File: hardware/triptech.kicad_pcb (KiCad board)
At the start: 4 copper layers, 262.8 x 99.5 mm, 75 parts, among them J1 Conn_01x03_Pin, J2 GPIO Header, J4 NCJ6FA-H-0, J5 NCJ6FA-H-0, J6 Conn_01x04_Pin, J7 NCJ6FA-H-0, J8 NCJ6FA-H-0, Q1 SI2301CDS-T1-GE3, U1 TMA-1212D, U2 TPS54302, U3 Daisy_Seed, U4 H11L1SM, U5 THAT1246, U6 THAT1246, U7 THAT1646, U8 THAT1646

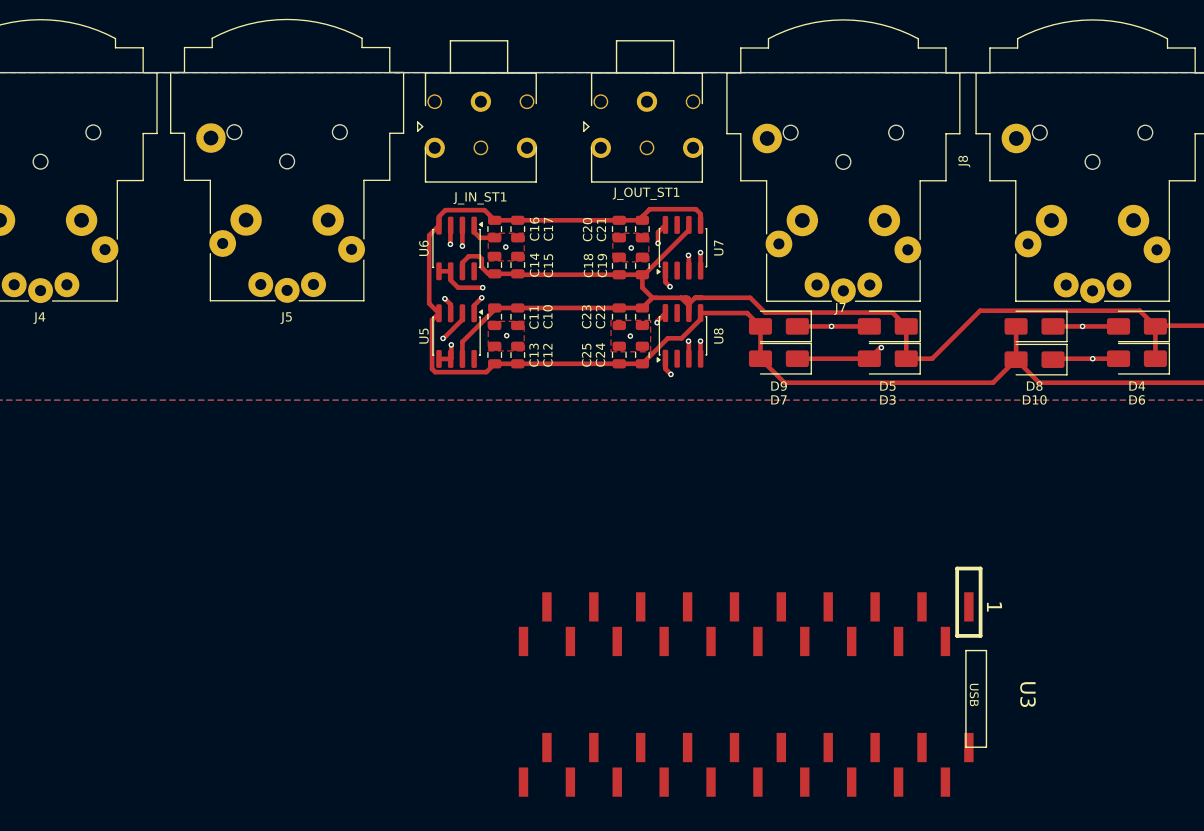
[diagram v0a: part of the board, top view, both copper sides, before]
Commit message: add protection circuit and repair pcb
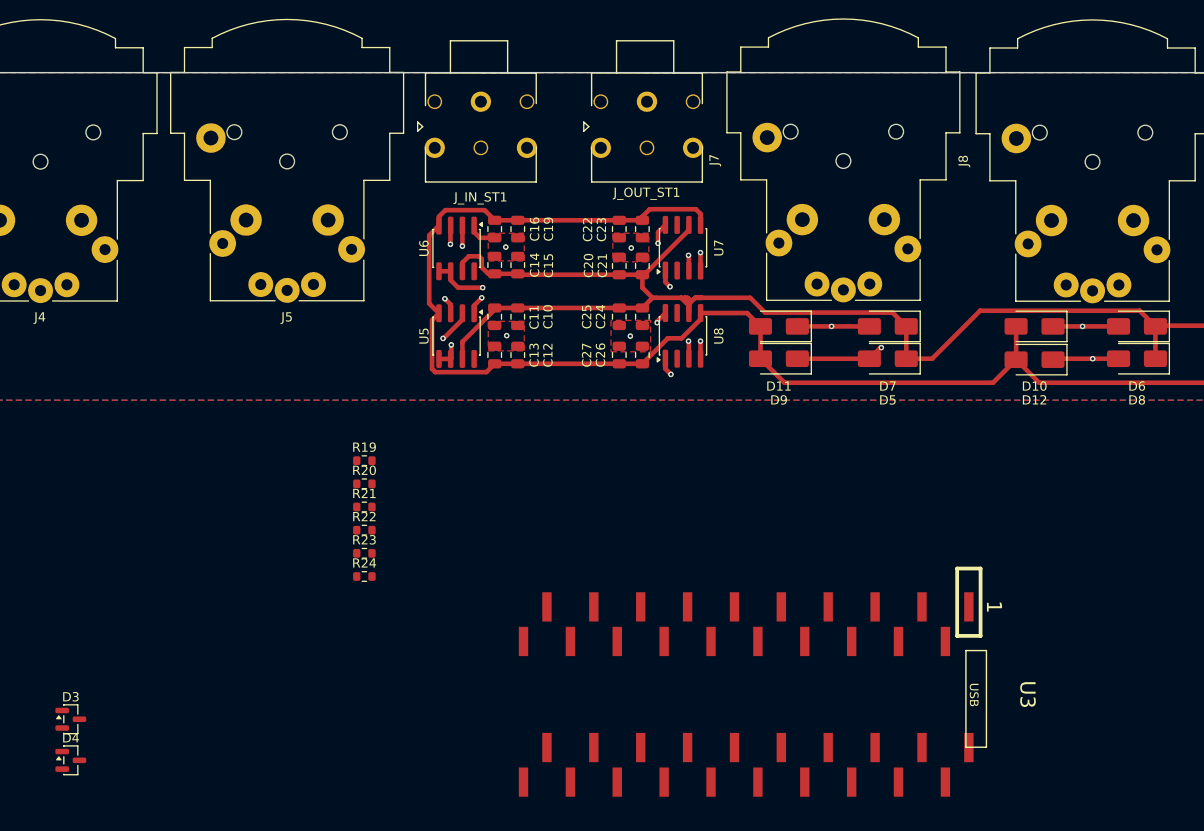
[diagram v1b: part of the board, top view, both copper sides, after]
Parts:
- added D3: BAT54S, Package_TO_SOT_SMD:SOT-23, F.Cu at (34.6, 90.1)
- added D4: BAT54S, Package_TO_SOT_SMD:SOT-23, F.Cu at (34.6, 94.5)
- added R19: 1.2k, Resistor_SMD:R_0603_1608Metric, F.Cu at (66.4, 62.0)
- added R20: 1.2k, Resistor_SMD:R_0603_1608Metric, F.Cu at (66.4, 64.6)
- added R21: 100k, Resistor_SMD:R_0603_1608Metric, F.Cu at (66.4, 67.1)
- added R22: 100k, Resistor_SMD:R_0603_1608Metric, F.Cu at (66.4, 69.6)
- added R23: 100k, Resistor_SMD:R_0603_1608Metric, F.Cu at (66.4, 72.1)
- added R24: 100k, Resistor_SMD:R_0603_1608Metric, F.Cu at (66.4, 74.6)
- moved J7 0.10 mm to (111.3, 38.5)
- renumbered C17 to C19, C18 to C20, C19 to C21, C20 to C22, C21 to C23, C22 to C24, C23 to C25, C24 to C26, C25 to C27, D8 to D10, D9 to D11, D10 to D12, D3 to D5, D4 to D6, D5 to D7, D6 to D8, D7 to D9
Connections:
- D11 pad 1: Net-(D5-A) (its old number) -> GNDA
- D12 pad 1: Net-(D10-K) (its old number) -> GNDA
- D7 pad 2: Net-(D5-A) (its old number) -> GNDA
- D8 pad 2: Net-(D10-K) (its old number) -> GNDA
- J7 pad 3: Net-(D5-A) (its old number) -> GNDA
- J7 pad R: Net-(D5-A) (its old number) -> GNDA
- J8 pad 3: Net-(D10-K) (its old number) -> GNDA
- J8 pad R: Net-(D10-K) (its old number) -> GNDA
- J_IN_ST1 pad 2: AUDIO_IN_L -> Net-(J_IN_ST1-T)
- J_IN_ST1 pad 5: AUDIO_IN_R -> Net-(J_IN_ST1-R)
- U5 pad 5: AUDIO_IN_L -> Net-(J_IN_ST1-T)
- U5 pad 6: AUDIO_IN_L -> Net-(J_IN_ST1-T)
- U6 pad 5: AUDIO_IN_R -> Net-(J_IN_ST1-R)
- U6 pad 6: AUDIO_IN_R -> Net-(J_IN_ST1-R)
- U7 pad 8: Net-(D5-A) (its old number) -> GNDA
- U8 pad 8: Net-(D10-K) (its old number) -> GNDA
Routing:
- net GNDA: track 8.79 -> 128.2 mm, vias 7 -> 11
- net Net-(D10-K) (its old number): track 75.3 -> 0.00 mm, vias 2 -> 0
- net Net-(D5-A) (its old number): track 44.0 -> 0.00 mm, vias 2 -> 0

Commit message: wip
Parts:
- added C17: 10u, Capacitor_SMD:C_0805_2012Metric, F.Cu at (35.8, 58.0)
- added C18: 10u, Capacitor_SMD:C_0805_2012Metric, F.Cu at (66.0, 54.5)
- added J_MIDI_IN1: SDS-50J, libs:SDS50J, F.Cu at (215.7, 38.7)
- added J_MIDI_OUT1: SDS-50J, libs:SDS50J, F.Cu at (192.9, 38.7)
- added J_MIDI_THRU1: SDS-50J, libs:SDS50J, F.Cu at (170.2, 38.7)
- added R25: 120R, Resistor_SMD:R_0603_1608Metric, F.Cu at (97.0, 39.8)
- added R26: 120R, Resistor_SMD:R_0603_1608Metric, F.Cu at (86.2, 39.7)
- added S1: LC2255EESP, libs:LC2255EESP, F.Cu at (90.2, 37.1)
- D2: value 1N4148WS -> 1N4148W; footprint Diode_SMD:D_SOD-323 -> Diode_SMD:D_SOD-123
- moved U3 128.6 mm to (258.1, 102.6)
- moved J6 72.8 mm to (90.3, 43.9)
- moved R8 68.0 mm to (255.4, 97.8), turned to -90 degrees
- moved C9 67.7 mm to (235.8, 45.8), turned to -90 degrees
- moved R7 66.3 mm to (252.8, 97.9), turned to -90 degrees
- moved R11 59.9 mm to (250.5, 97.7), turned to -90 degrees
- moved R10 59.4 mm to (247.9, 97.8), turned to -90 degrees
- moved C10 58.8 mm to (25.9, 60.5), turned to 90 degrees
- moved U4 58.4 mm to (229.9, 46.5)
- moved R9 57.5 mm to (245.3, 97.7), turned to -90 degrees
- moved C12 57.4 mm to (25.9, 56.5), turned to 90 degrees
- moved D2 55.8 mm to (219.2, 45.4)
- moved U5 55.3 mm to (22.0, 58.5)
- moved C11 54.3 mm to (28.1, 60.5), turned to 90 degrees
- moved C13 52.8 mm to (28.1, 56.5), turned to 90 degrees
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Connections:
- R13 pad 1: Net-(J_MIDI_OUT1-Pad5) -> GND
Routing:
- net -12VA: track 151.8 -> 0.00 mm
- net +12VA: track 138.6 -> 0.00 mm
- net GNDA: track 128.2 -> 0.00 mm, vias 11 -> 2
- net AUDIO_IN_L: track 119.4 -> 0.00 mm, vias 1 -> 0
- net AUDIO_IN_R: track 110.7 -> 0.00 mm, vias 1 -> 0
- net AUDIO_OUT_L: track 93.0 -> 0.00 mm, vias 1 -> 0
- net AUDIO_OUT_R: track 90.6 -> 0.00 mm, vias 1 -> 0
- net Net-(D10-K): track 85.5 -> 0.00 mm, vias 2 -> 0
- net Net-(U5-In+): track 55.9 -> 0.00 mm, vias 1 -> 0
- net Net-(D5-A): track 54.4 -> 0.00 mm, vias 2 -> 0
- net Net-(U5-In-): track 49.9 -> 0.00 mm, vias 1 -> 0
- net Net-(U6-In+): track 26.1 -> 0.00 mm, vias 1 -> 0
- net Net-(U6-In-): track 24.1 -> 0.00 mm, vias 1 -> 0
- removed copper zone on B.Cu, net GND
- removed copper zone on B.Cu, net GNDA
- removed copper zone on F.Cu, net GNDA

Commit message: PCB Assembledish Design checks next
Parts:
- removed R_STAR1: 0R, Resistor_THT:R_Axial_DIN0207_L6.3mm_D2.5mm_P5.08mm_Vertical
- added H1: MountingHole, MountingHole:MountingHole_3.2mm_M3, F.Cu at (20.0, 86.0)
- added H2: MountingHole, MountingHole:MountingHole_3.2mm_M3, F.Cu at (80.0, 86.0)
- added H3: MountingHole, MountingHole:MountingHole_3.2mm_M3, F.Cu at (160.2, 61.0)
- added H4: MountingHole, MountingHole:MountingHole_3.2mm_M3, F.Cu at (280.0, 86.0)
- added H5: MountingHole, MountingHole:MountingHole_3.2mm_M3, F.Cu at (280.0, 31.0)
- added J10: Earth, MountingHole:MountingHole_3.2mm_M3_Pad_Via, F.Cu at (20.0, 31.0)
- added J3: Micro_SD_Card, Connector_Card:microSD_HC_Hirose_DM3AT-SF-PEJM5, F.Cu at (249.9, 34.5)
- added J7: Earth, MountingHole:MountingHole_3.2mm_M3_Pad_Via, F.Cu at (80.0, 31.0)
- added JP1: Earth-Gnd Disconnect, Jumper:SolderJumper-2_P1.3mm_Bridged_Pad1.0x1.5mm, B.Cu at (136.9, 49.9)
- added L1: BLM18PG121SN1, Inductor_SMD:L_0603_1608Metric, F.Cu at (280.3, 65.6)
- added L2: BLM18PG121SN1, Inductor_SMD:L_0603_1608Metric, F.Cu at (280.4, 69.1)
- J1: value Conn_01x03_Pin -> Power; footprint Connector_PinHeader_2.54mm:PinHeader_1x03_P2.54mm_Vertical -> Connector_PinHeader_2.54mm:PinHeader_2x04_P2.54mm_Vertical
- U3: footprint Daisy-Boards:DAISY_SEED_SMT -> daisy:DAISY_SEED_SMT
- moved J1 110.2 mm to (270.1, 84.1), turned to -90 degrees
- moved J6 76.3 mm to (166.7, 45.5), turned to -90 degrees
- moved J_IN_ST1 74.4 mm to (153.2, 34.3)
- moved U3 62.7 mm to (216.4, 55.7)
- moved J_OUT_ST1 62.1 mm to (166.6, 34.3)
- moved J2 58.1 mm to (241.2, 76.5), turned to -90 degrees
- moved R9 56.7 mm to (201.9, 61.2), turned to 90 degrees
- moved R11 56.7 mm to (207.2, 61.2), turned to 90 degrees
- moved R8 56.5 mm to (212.2, 61.3), turned to 90 degrees
- moved R10 56.2 mm to (205.2, 61.2), turned to 90 degrees
- moved R26 56.1 mm to (141.5, 48.8)
- moved R7 56.1 mm to (210.3, 61.3), turned to 90 degrees
- moved D6 51.7 mm to (107.8, 67.5)
- moved S1 50.2 mm to (140.0, 42.9)
- moved R25 49.1 mm to (145.3, 48.4)
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- renumbered J7 to J8, J8 to J9, J_MIDI_IN1 to J_MIDI_IN_1, J_MIDI_OUT1 to J_MIDI_OUT_1, L1 to L3
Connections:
- C1 pad 1: -12VA -> Net-(U1--Vout)
- C1 pad 2: GNDA -> GND
- C10 pad 2: GNDA -> GND
- C11 pad 2: GNDA -> GND
- C12 pad 1: GNDA -> GND
- C13 pad 1: GNDA -> GND
- C14 pad 2: GNDA -> GND
- C15 pad 2: GNDA -> GND
- C16 pad 1: GNDA -> GND
- C19 pad 1: GNDA -> GND
- C2 pad 1: +12VA -> Net-(U1-+Vout)
- C2 pad 2: GNDA -> GND
- C20 pad 2: GNDA -> GND
- C21 pad 2: GNDA -> GND
- C22 pad 1: GNDA -> GND
- C23 pad 1: GNDA -> GND
- C24 pad 2: GNDA -> GND
- C25 pad 2: GNDA -> GND
- C26 pad 1: GNDA -> GND
- C27 pad 1: GNDA -> GND
- D11 pad 1: GNDA -> Net-(D11-K)
- D12 pad 1: GNDA -> Net-(D12-K)
- D3 pad 1: GNDA -> GND
- D3 pad 2: +5v -> +5V
- D4 pad 1: GNDA -> GND
- D4 pad 2: +5v -> +5V
- D7 pad 2: GNDA -> Net-(D11-K)
- D8 pad 2: GNDA -> Net-(D12-K)
- J1 pad 1: +12VA -> +5V
- J1 pad 2: GNDA -> +12VA
- J1 pad 3: -12VA -> GND
- J2 pad 1: GPIO_D12 -> GPIO_D0
- J2 pad 11: GPIO_D7 -> GPIO_D11
- J2 pad 13: GPIO_D0 -> GPIO_D12
- J2 pad 3: GPIO_D11 -> GPIO_D7
- J2 pad 5: GPIO_D10 -> GPIO_D8
- J2 pad 9: GPIO_D8 -> GPIO_D10
- J4 pad 1: GNDA -> Earth
- J4 pad G: GNDA -> Earth
- J4 pad S: GNDA -> Earth
- J5 pad 1: GNDA -> Earth
- J5 pad G: GNDA -> Earth
- J5 pad S: GNDA -> Earth
- J8 pad 1: GNDA -> Earth
- J8 pad 3: GNDA -> Net-(D11-K)
- J8 pad G: GNDA -> Earth
- J8 pad R: GNDA -> Net-(D11-K)
- J8 pad S: GNDA -> Earth
- J9 pad 1: GNDA -> Earth
- J9 pad 3: GNDA -> Net-(D12-K)
- J9 pad G: GNDA -> Earth
- J9 pad R: GNDA -> Net-(D12-K)
- J9 pad S: GNDA -> Earth
- J_IN_ST1 pad 1: GNDA -> GND
- J_MIDI_IN_1 pad MH1: unconnected-(J_MIDI_IN1-PadMH1) -> GND
- J_MIDI_IN_1 pad MH2: unconnected-(J_MIDI_IN1-PadMH2) -> GND
- J_MIDI_IN_1 pad MH3: unconnected-(J_MIDI_IN1-PadMH3) -> GND
- J_MIDI_IN_1 pad MH4: unconnected-(J_MIDI_IN1-PadMH4) -> GND
- J_MIDI_OUT_1 pad 5: GND -> Net-(J_MIDI_OUT_1-Pad5)
- J_MIDI_OUT_1 pad MH1: unconnected-(J_MIDI_OUT1-PadMH1) -> GND
- J_MIDI_OUT_1 pad MH2: unconnected-(J_MIDI_OUT1-PadMH2) -> GND
- J_MIDI_OUT_1 pad MH3: unconnected-(J_MIDI_OUT1-PadMH3) -> GND
- J_MIDI_OUT_1 pad MH4: unconnected-(J_MIDI_OUT1-PadMH4) -> GND
- J_MIDI_THRU1 pad MH1: unconnected-(J_MIDI_THRU1-PadMH1) -> GND
- J_MIDI_THRU1 pad MH2: unconnected-(J_MIDI_THRU1-PadMH2) -> GND
- J_MIDI_THRU1 pad MH3: unconnected-(J_MIDI_THRU1-PadMH3) -> GND
- J_MIDI_THRU1 pad MH4: unconnected-(J_MIDI_THRU1-PadMH4) -> GND
- J_OUT_ST1 pad 1: GNDA -> GND
- R13 pad 1: GND -> Net-(J_MIDI_OUT_1-Pad5)
- R21 pad 2: +5v -> +5V
- R22 pad 1: GNDA -> GND
- R23 pad 2: +5v -> +5V
- R24 pad 1: GNDA -> GND
- R25 pad 2: GNDA -> GND
- R26 pad 2: GNDA -> GND
- S1 pad MH1: unconnected-(S1-PadMH1) -> GND
- S1 pad MH2: unconnected-(S1-PadMH2) -> GND
- U1 pad 2: GNDA -> GND
- U1 pad 4: -12VA -> Net-(U1--Vout)
- U1 pad 5: GNDA -> GND
- U1 pad 6: +12VA -> Net-(U1-+Vout)
- U3 pad 20: GNDA -> GND
- U5 pad 1: GNDA -> GND
- U6 pad 1: GNDA -> GND
- U7 pad 3: GNDA -> GND
- U7 pad 8: GNDA -> Net-(D11-K)
- U8 pad 3: GNDA -> GND
- U8 pad 8: GNDA -> Net-(D12-K)
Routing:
- net +12VA: track 0.00 -> 429.5 mm, vias 0 -> 13
- net -12VA: track 0.00 -> 404.0 mm, vias 0 -> 12
- net +5V: track 0.00 -> 313.3 mm, vias 0 -> 8
- net +3V3D: track 0.00 -> 198.3 mm, vias 0 -> 6
- net AUDIO_IN_L: track 0.00 -> 184.2 mm
- net Net-(J_IN_ST1-T): track 0.00 -> 162.6 mm, vias 0 -> 1
- net AUDIO_IN_R: track 0.00 -> 145.2 mm, vias 0 -> 2
- net Net-(J_IN_ST1-R): track 0.00 -> 143.5 mm, vias 0 -> 1
- net Net-(S1-NO_1): track 0.00 -> 126.1 mm, vias 0 -> 2
- net Net-(S1-NO_2): track 0.00 -> 122.8 mm
- net +3V3A: track 0.00 -> 105.5 mm, vias 0 -> 1
- net GPIO_D15: track 0.00 -> 101.8 mm
- net GPIO_D16: track 0.00 -> 91.8 mm
- net GPIO_D17: track 0.00 -> 88.3 mm
- net Net-(D5-A): track 0.00 -> 82.6 mm
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- added copper zone on B.Cu, net Earth
- added copper zone on In1.Cu, net Earth
- added copper zone on B.Cu, net GND
- added copper zone on In1.Cu, net GND
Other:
- board size 262.8 x 99.5 mm -> 270 x 65 mm

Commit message: Stitch WIP
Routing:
- net +5V: track 313.3 -> 312.3 mm
- net GND: vias 39 -> 896
- net Earth: vias 1 -> 207

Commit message: PCB rev 1
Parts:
- moved H1 64.6 mm to (59.1, 137.4)
- moved H4 64.6 mm to (319.1, 137.4)
- moved R13 64.6 mm to (257.2, 96.6)
- moved R14 64.6 mm to (265.7, 96.6)
- moved C20 64.6 mm to (165.5, 119.6)
- moved C3 64.6 mm to (315.1, 101.3)
- moved D10 64.6 mm to (146.9, 115.4)
- moved D11 64.6 mm to (139.5, 115.4)
- moved D12 64.6 mm to (154.2, 115.4)
- moved D9 64.6 mm to (132.2, 115.4)
- moved H3 64.6 mm to (59.6, 77.8)
- moved J5 64.6 mm to (95.4, 96.1)
- moved J8 64.6 mm to (128.8, 96.1)
- moved J9 64.6 mm to (155.5, 96.1)
- moved JP1 64.6 mm to (176.0, 101.3)
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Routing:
- net GND: track 72.6 -> 76.0 mm, vias 896 -> 889
- net GPIO_D7: track 65.4 -> 65.5 mm, vias 0 -> 2
